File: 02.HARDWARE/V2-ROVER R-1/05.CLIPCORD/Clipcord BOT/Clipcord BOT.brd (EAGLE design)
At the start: 20 x 13 mm, 0 parts

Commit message: primera version para DanKubin model  - pedido a PCBWAY
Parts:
- added TP1, TP2, TP3: TESTPAD_TPSQB1,27, BeagleBone_Blue_R3:TESTPAD_B1,27
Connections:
- new net LINE: TP1.TP, TP2.TP, TP3.TP
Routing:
- net LINE: track 0.00 -> 9.48 mm, vias 0 -> 1
- added copper zone on layer 1, net LINE
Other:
- board text added: "MUSOTOKU"

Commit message: se cambia la forma exterior (WIP)
No esta terminado
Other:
- board size 20 x 13 mm -> 20.6 x 29.3 mm

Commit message: v2. Revisada.
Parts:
- moved TP1 61.9 mm to (41.4, 30.3)
- moved TP2 61.9 mm to (50.4, 30.3)
- moved TP3 61.9 mm to (52.4, 30.3)
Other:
- board size 20.6 x 29.3 mm -> 20.7 x 12.8 mm

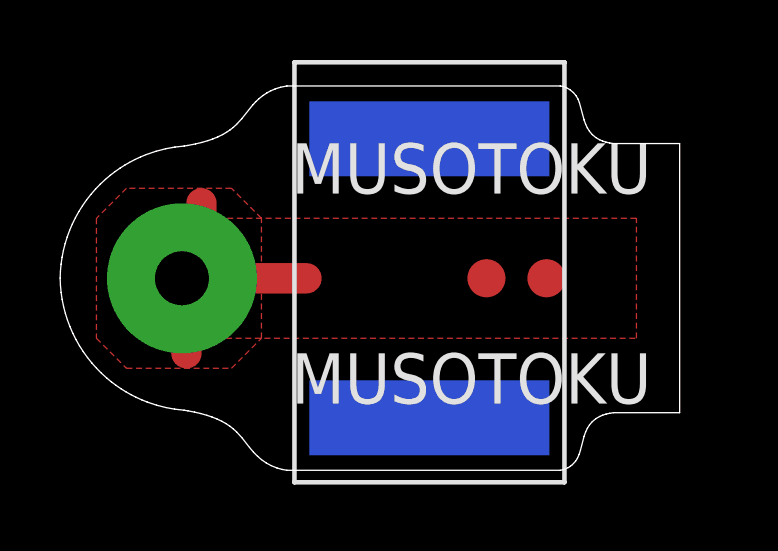
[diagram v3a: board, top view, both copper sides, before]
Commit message: Modificacion del Clipcord 3
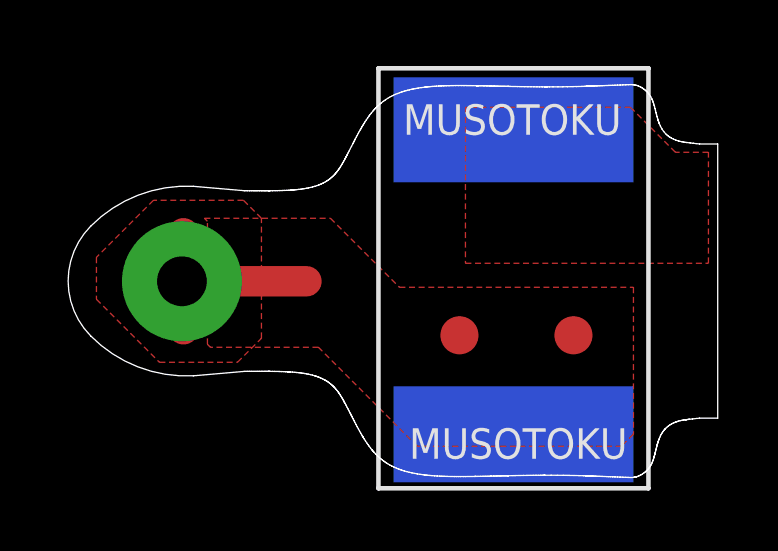
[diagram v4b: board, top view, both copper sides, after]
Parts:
- moved TP2 3.47 mm to (53.3, 28.4)
- moved TP3 3.47 mm to (49.5, 28.4)
- moved TP1 1.10 mm to (40.3, 30.3)
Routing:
- net LINE: track 9.48 -> 7.39 mm
- added copper zone on layer 1, net N$1
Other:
- board size 20.7 x 12.8 mm -> 21.7 x 13.1 mm

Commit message: Cambios menores antes de pedido
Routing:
- net LINE: track 7.39 -> 32.4 mm
- added copper zone on layer 16, net N$2

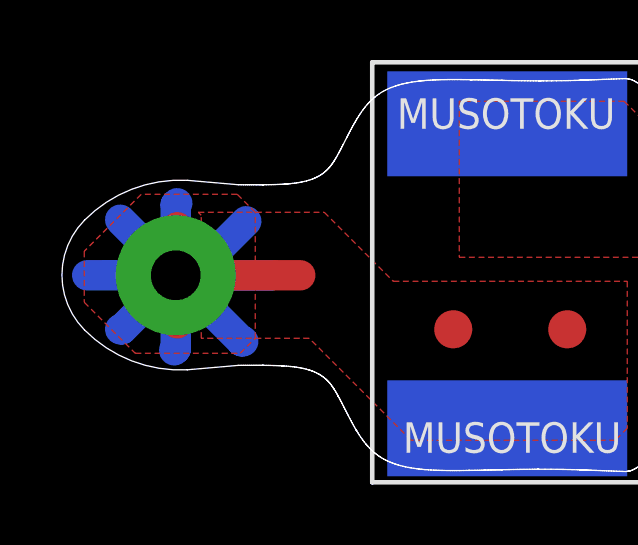
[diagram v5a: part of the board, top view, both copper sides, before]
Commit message: Se mueve el taladro del pin mas cerca del borde
Se mueve el taladro del pin mas cerca del borde tras las pruebas en Intattoo Veritas  porque  se comprueba que para algunas máquinas de bobinas el agujero esta tan cerca del chasis que toca
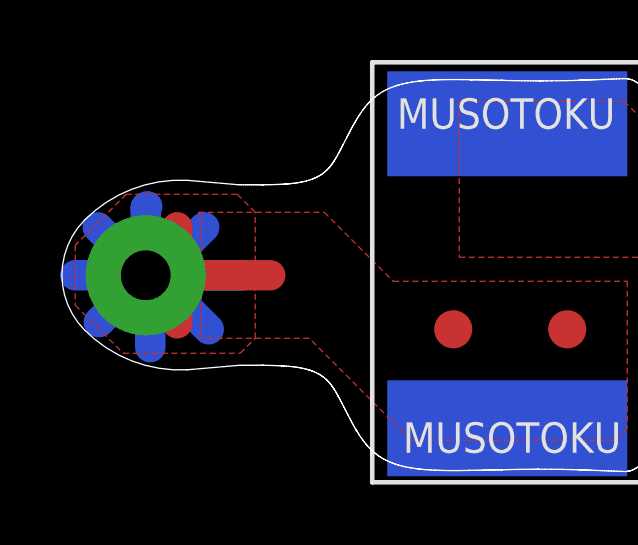
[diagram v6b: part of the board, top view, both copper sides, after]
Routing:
- net LINE: track 32.4 -> 30.1 mm
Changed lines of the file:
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@@
 <grid distance="0.1" unitdist="mm" unit="mm" style="lines" multiple="1" display="yes" altdistance="5" altunitdist="mil" altunit="mil"/>
 <layers>
-<layer number="1" name="Top" color="4" fill="1" visible="yes" active="yes"/>
+<layer number="1" name="Top" color="4" fill="1" visible="no" active="yes"/>
 <layer number="2" name="Route2" color="16" fill="1" visible="no" active="no"/>
 <layer number="15" name="Route15" color="23" fill="1" visible="no" active="no"/>
@@
 <layer number="19" name="Unrouted" color="6" fill="1" visible="yes" active="yes"/>
 <layer number="20" name="Dimension" color="24" fill="1" visible="yes" active="yes"/>
-<layer number="21" name="tPlace" color="7" fill="1" visible="no" active="yes"/>
+<layer number="21" name="tPlace" color="7" fill="1" visible="yes" active="yes"/>
 <layer number="22" name="bPlace" color="7" fill="1" visible="yes" active="yes"/>
 <layer number="23" name="tOrigins" color="15" fill="1" visible="no" active="yes"/>
@@
 <contactref element="TP2" pad="TP"/>
 <polygon width="0.254" layer="1" isolate="0.5" rank="2">
-<vertex x="39.1" y="32.9"/>
-<vertex x="37.2" y="31"/>
-<vertex x="37.2" y="29.3"/>
-<vertex x="38.9" y="27.6"/>
+<vertex x="38.6" y="32.9"/>
+<vertex x="36.9" y="31.2"/>
+<vertex x="36.9" y="29.2"/>
+<vertex x="38.5" y="27.6"/>
 <vertex x="42.4" y="27.6"/>
 <vertex x="42.9" y="28.1"/>
@@
 <vertex x="42.3" y="32.9"/>
 </polygon>
-<via x="40.25" y="30.2" extent="1-16" drill="1.66" diameter="4"/>
-<wire x1="40.25" y1="30.2" x2="44.4" y2="30.2" width="1.016" layer="1"/>
-<wire x1="40.25" y1="30.2" x2="40.3" y2="30.25" width="1.016" layer="1"/>
-<wire x1="40.3" y1="30.25" x2="40.3" y2="31.8" width="1.016" layer="1"/>
-<wire x1="40.25" y1="30.2" x2="40.3" y2="30.15" width="1.016" layer="1"/>
-<wire x1="40.3" y1="30.15" x2="40.3" y2="28.6" width="1.016" layer="1"/>
+<via x="39.25" y="30.2" extent="1-16" drill="1.66" diameter="4"/>
+<wire x1="39.25" y1="30.2" x2="43.4" y2="30.2" width="1.016" layer="1"/>
+<wire x1="39.25" y1="30.2" x2="40.3" y2="31.25" width="1.016" layer="1"/>
+<wire x1="40.3" y1="31.25" x2="40.3" y2="31.8" width="1.016" layer="1"/>
+<wire x1="39.25" y1="30.2" x2="40.3" y2="29.15" width="1.016" layer="1"/>
+<wire x1="40.3" y1="29.15" x2="40.3" y2="28.6" width="1.016" layer="1"/>
 <contactref element="TP3" pad="TP"/>
 <polygon width="0.2" layer="1">
@@
 <vertex x="41.1" y="32.2"/>
 </polygon>
-<wire x1="38.4" y1="32.05" x2="38.4" y2="32.1" width="0.8128" layer="16"/>
-<wire x1="40.25" y1="30.2" x2="40.15" y2="30.3" width="0.8128" layer="16"/>
-<wire x1="40.15" y1="30.3" x2="37.9" y2="30.3" width="0.8128" layer="16"/>
-<wire x1="40.25" y1="30.2" x2="43.5" y2="30.2" width="1.016" layer="16"/>
-<wire x1="40.25" y1="30.2" x2="40.8" y2="30.2" width="1.016" layer="16"/>
-<wire x1="40.8" y1="30.2" x2="42.6" y2="32" width="1.016" layer="16"/>
-<wire x1="40.25" y1="30.2" x2="38.45" y2="28.4" width="1.016" layer="16"/>
-<wire x1="38.45" y1="28.4" x2="38.4" y2="28.4" width="1.016" layer="16"/>
-<wire x1="40.25" y1="30.2" x2="42.45" y2="28" width="1.016" layer="16"/>
-<wire x1="42.45" y1="28" x2="42.5" y2="28" width="1.016" layer="16"/>
-<wire x1="40.25" y1="30.2" x2="40.25" y2="27.75" width="1.016" layer="16"/>
-<wire x1="40.25" y1="27.75" x2="40.2" y2="27.7" width="1.016" layer="16"/>
-<wire x1="40.25" y1="30.2" x2="37.3" y2="30.2" width="1.016" layer="16"/>
-<wire x1="40.25" y1="30.2" x2="38.4" y2="32.05" width="1.016" layer="16"/>
-<wire x1="40.25" y1="30.2" x2="40.25" y2="32.55" width="1.016" layer="16"/>
-<wire x1="40.25" y1="32.55" x2="40.3" y2="32.6" width="1.016" layer="16"/>
+<wire x1="37.65" y1="31.8" x2="37.6" y2="31.8" width="0.8128" layer="16"/>
+<wire x1="39.25" y1="30.2" x2="39.15" y2="30.3" width="0.8128" layer="16"/>
+<wire x1="39.15" y1="30.3" x2="37.9" y2="30.3" width="0.8128" layer="16"/>
+<wire x1="39.25" y1="30.2" x2="42.5" y2="30.2" width="1.016" layer="16"/>
+<wire x1="39.25" y1="30.2" x2="39.6" y2="30.2" width="1.016" layer="16"/>
+<wire x1="39.6" y1="30.2" x2="41.2" y2="31.8" width="1.016" layer="16"/>
+<wire x1="39.25" y1="30.2" x2="39.4" y2="30.2" width="1.016" layer="16"/>
+<wire x1="39.25" y1="30.2" x2="37.6875" y2="28.6375" width="1.016" layer="16"/>
+<wire x1="41.35" y1="28.4" x2="39.55" y2="30.2" width="1.016" layer="16"/>
+<wire x1="39.25" y1="30.2" x2="39.55" y2="30.2" width="1.016" layer="16"/>
+<wire x1="39.4" y1="30.2" x2="39.4" y2="27.8" width="1.016" layer="16"/>
+<wire x1="39.25" y1="30.2" x2="36.9" y2="30.2" width="1.016" layer="16"/>
+<wire x1="39.25" y1="30.2" x2="37.65" y2="31.8" width="1.016" layer="16"/>
+<wire x1="39.25" y1="30.2" x2="39.25" y2="32.45" width="1.016" layer="16"/>
+<wire x1="39.25" y1="32.45" x2="39.3" y2="32.5" width="1.016" layer="16"/>
 </signal>
 <signal name="N$1">
